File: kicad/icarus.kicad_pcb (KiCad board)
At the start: 2 copper layers, 7.5 x 2 mm, 78 parts, among them J1 CAN Bus, J2 CAN Bus, J3 SWD Programming, J4 USB_B_Micro, Q1 BSS123, U1 MAX15062A, U10 XT30, U11 XT30, U12 XT30, U13 XT30, U14 LT1787HVIMS8PBF, U15 USBLC6-2SC6, U16 STLM20DD9FUDFN-4L_STM-L, U2 STM32G474CEU6, U3 TCAN334G, U4 ZXMP10A13FTA, U5 XT90, U6 FSV10150VTO277-3L_ONS-L, U7 XT30, U8 XT30, U9 TPS2490DGSR

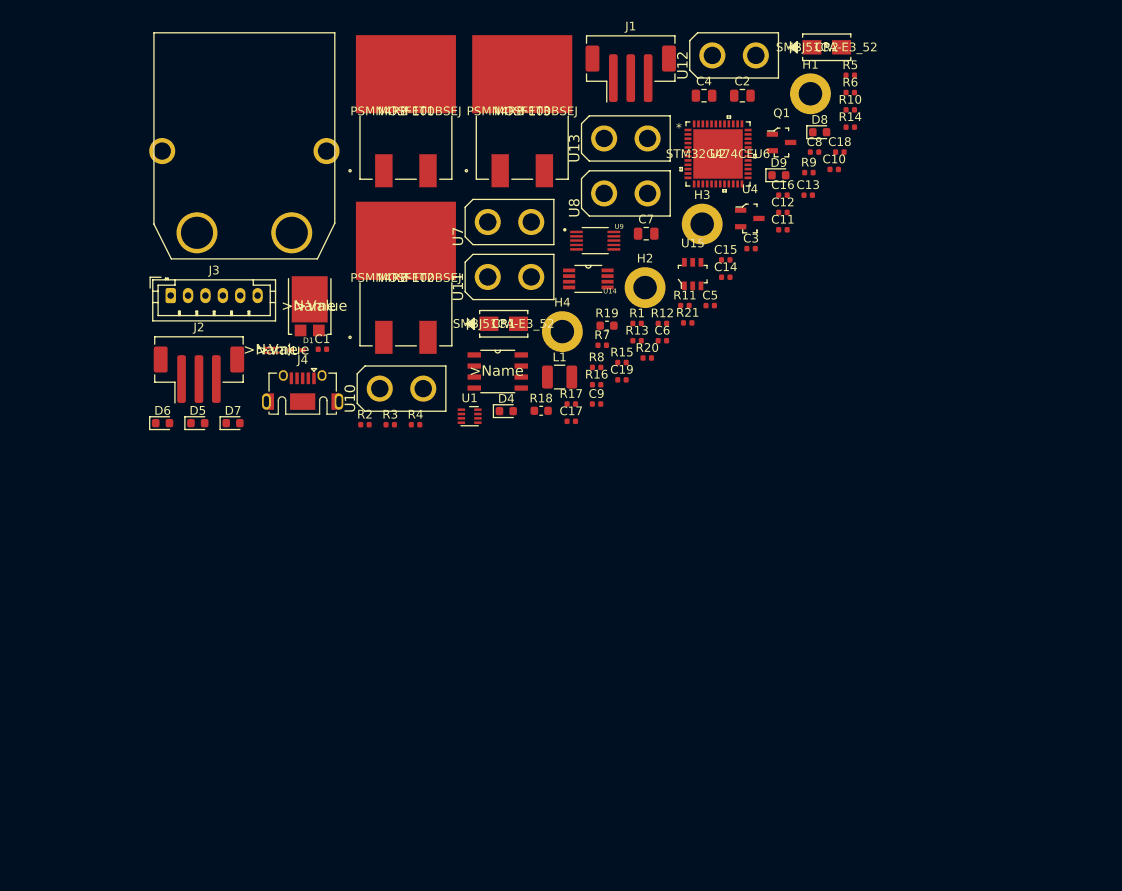
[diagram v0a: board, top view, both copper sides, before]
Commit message: Finished importing and modifying footprints
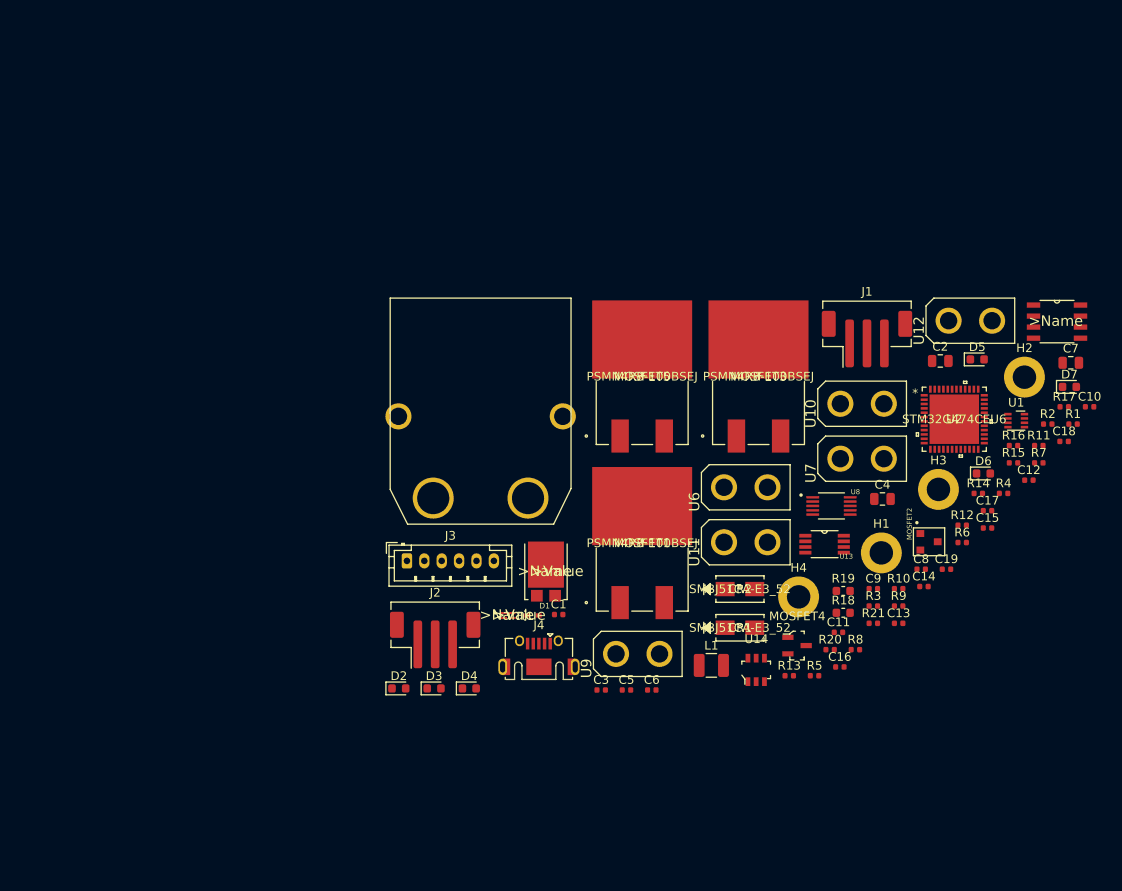
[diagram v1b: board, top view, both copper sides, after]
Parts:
- removed D8, D9: Blue, LED_SMD:LED_0603_1608Metric
- removed Q1: BSS123, digikey-footprints:SOT-23-3
- removed U16: STLM20DD9FUDFN-4L_STM-L, icarus_kicad_lib:STLM20DD9FUDFN-4L_STM-L
- added D2: Green, LED_SMD:LED_0603_1608Metric, F.Cu at (107.9, 116.0)
- added D3: Green, LED_SMD:LED_0603_1608Metric, F.Cu at (112.0, 116.0)
- added MOSFET4: BSS123, digikey-footprints:SOT-23-3, F.Cu at (153.7, 111.1)
- added MOSFET5: PSMN4R8-100BSEJ, icarus_kicad_lib:PSMN4R8-100BSEJ, F.Cu at (135.9, 80.1)
- D4, D5: value Green -> Blue
- MOSFET2: value PSMN4R8-100BSEJ -> ZXMP10A13FTA; footprint icarus_kicad_lib:PSMN4R8-100BSEJ -> icarus_kicad_lib:ZXMP10A13FTA
- R4: value 10 -> 100k
- R5: value 100k -> 220
- R7: value 220 -> 10
- U13: value XT30 -> LT1787HVIMS8PBF; footprint icarus_kicad_lib:XT30P -> icarus_kicad_lib:LT1787HVIMS8PBF
- U14: value LT1787HVIMS8PBF -> USBLC6-2SC6; footprint icarus_kicad_lib:LT1787HVIMS8PBF -> digikey-footprints:SOT-23-6
- U15: value USBLC6-2SC6 -> STLM20DD9FUDFN-4L_STM-L; footprint digikey-footprints:SOT-23-6 -> icarus_kicad_lib:STLM20DD9FUDFN-4L_STM-L
- U4: value ZXMP10A13FTA -> XT90; footprint digikey-footprints:SOT-23-3 -> icarus_kicad_lib:XT90PW-M
- U5: value XT90 -> FSV10150VTO277-3L_ONS-L; footprint icarus_kicad_lib:XT90PW-M -> icarus_kicad_lib:FSV10150VTO277-3L_ONS-L
- U6: value FSV10150VTO277-3L_ONS-L -> XT30; footprint icarus_kicad_lib:FSV10150VTO277-3L_ONS-L -> icarus_kicad_lib:XT30P
- U8: value XT30 -> TPS2490DGSR; footprint icarus_kicad_lib:XT30P -> icarus_kicad_lib:TPS2490DGSR
- U9: value TPS2490DGSR -> XT30; footprint icarus_kicad_lib:TPS2490DGSR -> icarus_kicad_lib:XT30P
- moved D7 96.3 mm to (185.0, 81.3)
- moved D6 94.6 mm to (175.1, 91.3)
- moved D5 89.9 mm to (174.4, 78.2)
- moved R2 78.5 mm to (182.5, 85.6)
- moved R5 69.2 mm to (155.7, 114.5)
- moved R4 68.1 mm to (177.5, 93.6)
- moved MOSFET2 67.4 mm to (168.9, 99.1)
- moved U3 64.6 mm to (183.6, 73.8)
- moved CR2 63.1 mm to (147.1, 104.6)
- moved U1 62.9 mm to (178.9, 85.2)
- moved R3 59.3 mm to (162.5, 106.5)
- moved R17 56.7 mm to (184.4, 83.6)
- moved MOSFET1 56.6 mm to (135.9, 99.3)
- moved R10 55.3 mm to (165.4, 104.5)
- moved C16 54.7 mm to (158.6, 113.5)
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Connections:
- R11 pad 1: Net-(D6-Pad1) -> Net-(D4-Pad1)
- R12 pad 1: Net-(D7-Pad1) -> Net-(D5-Pad1)
- R13 pad 1: Net-(D8-Pad1) -> Net-(D6-Pad1)
- R14 pad 1: Net-(D9-Pad1) -> Net-(D7-Pad1)
- R3 pad 1: Net-(R3-Pad1) -> Net-(MOSFET2-PadP$1)
- R4 pad 1: GATE -> Net-(MOSFET4-Pad3)
- R4 pad 2: Net-(MOSFET1-Pad1) -> Net-(MOSFET2-PadP$1)
- R5 pad 2: Net-(R3-Pad1) -> GND
- R6 pad 1: Net-(D4-Pad1) -> Net-(D3-Pad1)
- R7 pad 1: Net-(D5-Pad1) -> GATE
- R7 pad 2: GND -> Net-(MOSFET1-Pad1)
- R8 pad 1: Net-(R8-Pad1) -> Net-(MOSFET2-PadP$2)
- U13 pad 1: (no net) -> Net-(C15-Pad2)
- U13 pad 2: (no net) -> VSENSE_LOW
- U14 pad 1: Net-(C15-Pad2) -> USB_CONN_D-
- U14 pad 2: VSENSE_LOW -> GND
- U14 pad 3: Net-(U14-Pad3) -> USB_CONN_D+
- U14 pad 4: GND -> USB_D+
- U14 pad 5: I_SENSE -> +5V
- U14 pad 6: I_SENSE_BIAS -> USB_D-
- U15 pad 1: USB_CONN_D- -> MOSFET_TEMP
- U15 pad 2: GND -> Net-(U15-Pad2)
- U15 pad 3: USB_CONN_D+ -> GND
- U15 pad 4: USB_D+ -> +3V3
- U5 pad 1: (no net) -> GND
- U5 pad 2: (no net) -> GND
- U8 pad 1: (no net) -> EN
- U8 pad 2: (no net) -> Net-(R15-Pad1)
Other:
- outline, holes or cut-outs redrawn

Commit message: Initial rough layout done
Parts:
- J1, J2: footprint Connector_JST:JST_PH_B3B-PH-SM4-TB_1x03-1MP_P2.00mm_Vertical -> Connector_JST:JST_PH_B3B-PH-K_1x03_P2.00mm_Vertical
- moved U3 111.9 mm to (79.9, 115.8)
- moved D7 108.0 mm to (77.1, 85.6)
- moved R11 106.9 mm to (74.6, 88.3), turned to 180 degrees
- moved J1 102.0 mm to (67.8, 115.5), turned to 270 degrees
- moved R14 100.5 mm to (74.4, 85.6), turned to 180 degrees
- moved C10 100.0 mm to (91.7, 112.6), turned to 90 degrees
- moved H1 99.4 mm to (67.5, 126.5)
- moved C18 95.3 mm to (97.8, 127.4)
- moved R6 92.3 mm to (81.1, 87.8), turned to 180 degrees
- moved H4 89.1 mm to (67.2, 85.2)
- moved C12 86.4 mm to (99.6, 122.6)
- moved R12 84.4 mm to (89.2, 85.4), turned to 180 degrees
- moved U2 83.8 mm to (94.7, 117.9)
- moved D6 83.6 mm to (91.6, 87.9)
- moved D5 83.0 mm to (91.8, 85.5)
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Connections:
- C10 pad 2: Net-(C10-Pad2) -> GND
- C11 pad 2: Net-(C10-Pad2) -> GND
- C12 pad 2: Net-(C10-Pad2) -> GND
- C13 pad 2: Net-(C10-Pad2) -> GND
- C8 pad 2: Net-(C10-Pad2) -> GND
- C9 pad 2: Net-(C10-Pad2) -> GND
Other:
- outline, holes or cut-outs redrawn

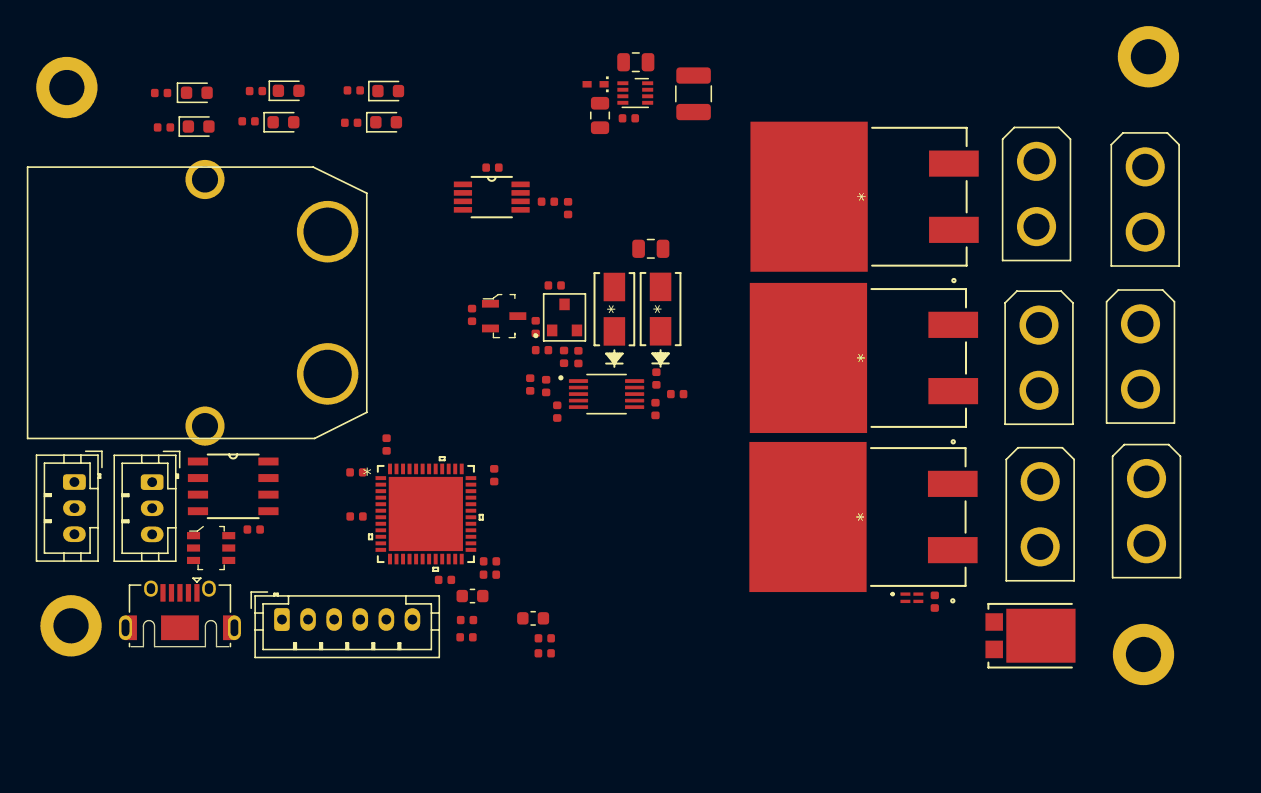
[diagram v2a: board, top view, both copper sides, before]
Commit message: Compressed board layout, about to start traces
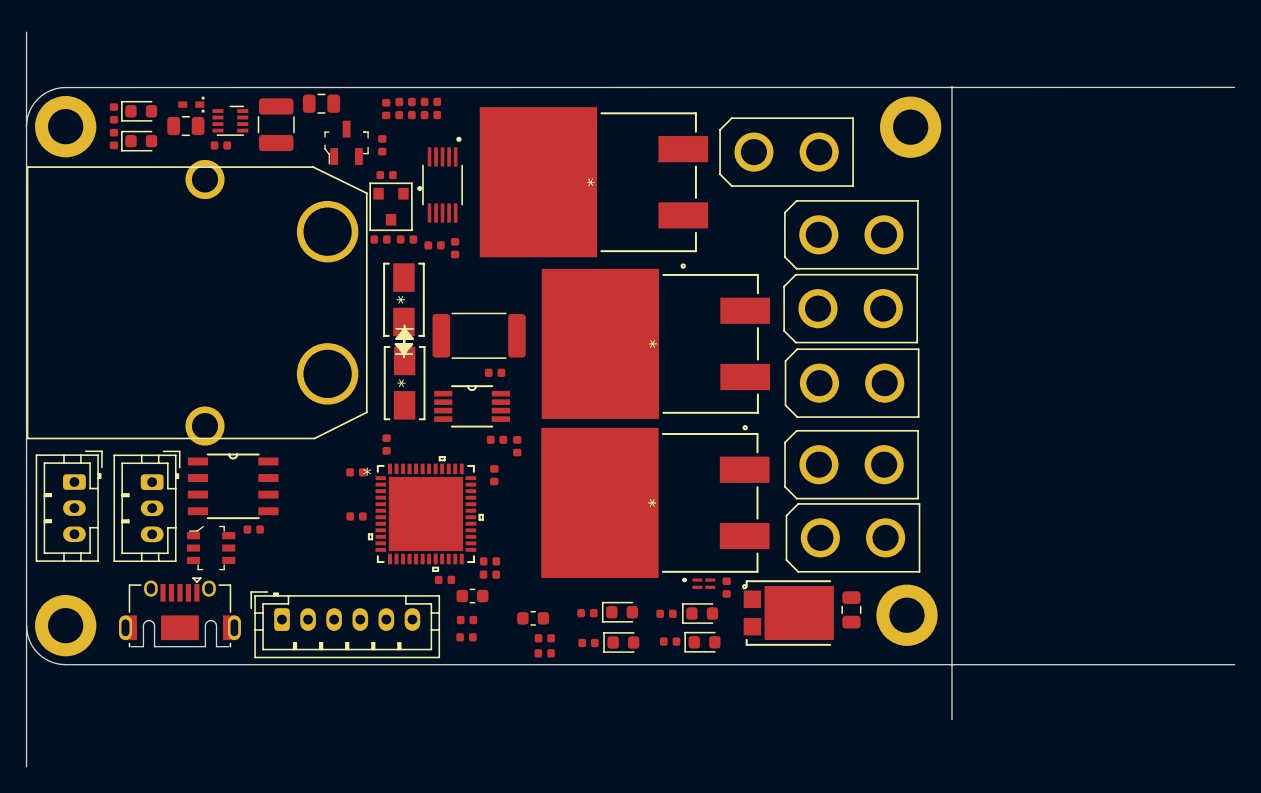
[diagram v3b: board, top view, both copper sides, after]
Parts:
- R1: footprint Resistor_SMD:R_0402_1005Metric -> Resistor_SMD:R_2512_6332Metric
- moved D7 55.6 mm to (115.9, 125.5)
- moved R14 55.6 mm to (113.1, 125.6)
- moved D4 49.4 mm to (109.7, 125.4)
- moved R11 49.4 mm to (107.1, 125.5)
- moved D5 48.7 mm to (116.1, 127.7)
- moved R12 48.7 mm to (113.4, 127.7)
- moved D6 43.8 mm to (109.8, 127.8)
- moved R13 43.8 mm to (107.2, 127.8)
- moved L1 32.1 mm to (83.2, 88.1)
- moved C4 31.8 mm to (76.3, 88.2), turned to 180 degrees
- moved C7 31.7 mm to (127.3, 125.3), turned to 270 degrees
- moved C3 31.3 mm to (79.0, 89.7)
- moved U1 31.1 mm to (79.7, 87.8)
- moved D1 31.0 mm to (76.8, 86.5)
- moved U12 27.7 mm to (122.3, 90.2), turned to 0 degrees
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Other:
- board size 7.5 x 2 mm -> 92.6 x 56.3 mm
- copper layers 2 -> 4

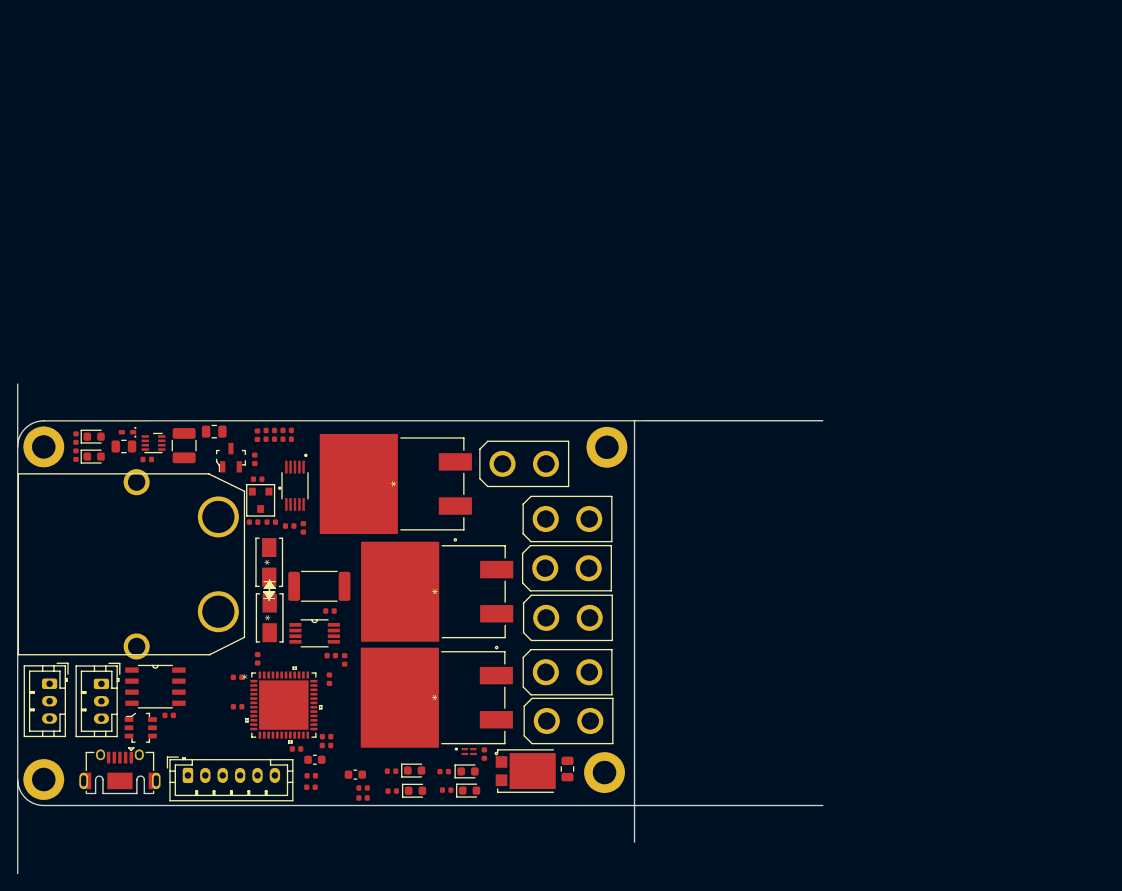
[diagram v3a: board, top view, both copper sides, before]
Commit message: Began initial routing
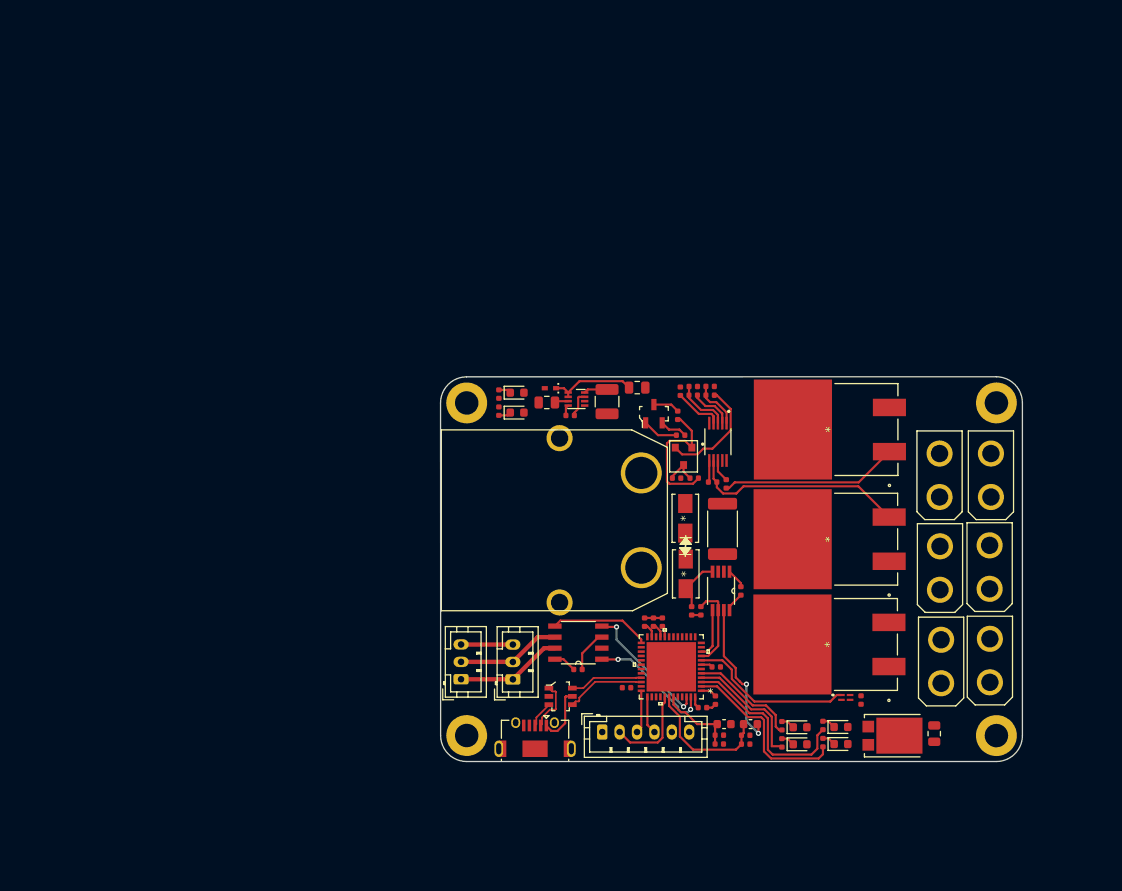
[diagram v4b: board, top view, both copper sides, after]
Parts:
- moved C5 55.2 mm to (144.4, 113.5), turned to 0 degrees
- moved J1 53.3 mm to (121.0, 115.0), turned to 90 degrees
- moved MOSFET3 50.3 mm to (157.5, 86.2)
- moved R18 50.3 mm to (148.4, 120.1)
- moved C18 50.2 mm to (147.8, 122.4)
- moved R20 50.2 mm to (147.8, 121.4)
- moved R11 49.7 mm to (156.7, 122.2), turned to 270 degrees
- moved D4 49.1 mm to (158.8, 122.4)
- moved U10 49.0 mm to (176.0, 91.5), turned to 90 degrees
- moved U7 49.0 mm to (175.9, 112.8), turned to 90 degrees
- moved L1 48.9 mm to (131.9, 83.0)
- moved R15 48.9 mm to (141.8, 82.3)
- moved R4 48.9 mm to (140.0, 84.6)
- moved U4 48.9 mm to (135.8, 96.7)
- moved U8 48.9 mm to (144.6, 87.6)
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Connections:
- U2 pad 11: LED1 -> Net-(U2-Pad11)
- U2 pad 13: LED2 -> Net-(U2-Pad13)
- U2 pad 15: LED3 -> Net-(U2-Pad15)
- U2 pad 17: LED4 -> Net-(U2-Pad17)
- U2 pad 18: 24V_SENSE -> Net-(U2-Pad18)
- U2 pad 19: VSW_SENSE -> Net-(U2-Pad19)
- U2 pad 2: Net-(U2-Pad2) -> LED1
- U2 pad 25: Net-(U2-Pad25) -> CAN_SHDN
- U2 pad 3: Net-(U2-Pad3) -> LED2
- U2 pad 4: Net-(U2-Pad4) -> LED3
- U2 pad 42: Net-(U2-Pad42) -> 24V_SENSE
- U2 pad 43: Net-(U2-Pad43) -> VSW_SENSE
- U2 pad 45: CAN_SHDN -> Net-(U2-Pad45)
- U2 pad 5: Net-(U2-Pad5) -> LED4
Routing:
- net VSENSE_HIGH: track 0.00 -> 31.0 mm, vias 0 -> 2
- net OUT: track 0.00 -> 25.2 mm
- net GND: track 0.00 -> 24.3 mm
- net LED2: track 0.00 -> 21.6 mm
- net LED1: track 0.00 -> 20.6 mm
- net Net-(MOSFET1-Pad1): track 0.00 -> 20.5 mm
- net MOSFET_TEMP: track 0.00 -> 19.0 mm
- net Net-(MOSFET2-PadP$1): track 0.00 -> 15.8 mm
- net 24V_SENSE: track 0.00 -> 15.4 mm
- net CAN_RX: track 0.00 -> 15.4 mm, vias 0 -> 2
- net LED3: track 0.00 -> 14.6 mm
- net CAN_TX: track 0.00 -> 14.5 mm, vias 0 -> 2
- net +3V3: track 0.00 -> 14.1 mm
- net Net-(MOSFET2-PadP$2): track 0.00 -> 12.8 mm
- net LED4: track 0.00 -> 12.7 mm
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- added copper zone on In2.Cu-3V3, net +3V3
- added copper zone on In1.Cu-GND, net GND
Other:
- board size 92.6 x 56.3 mm -> 66.9 x 44.2 mm
- rule trace_min: 0.2 -> 0.16
